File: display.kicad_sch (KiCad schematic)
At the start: 1 part, among them J7 FFC3B11-40-T

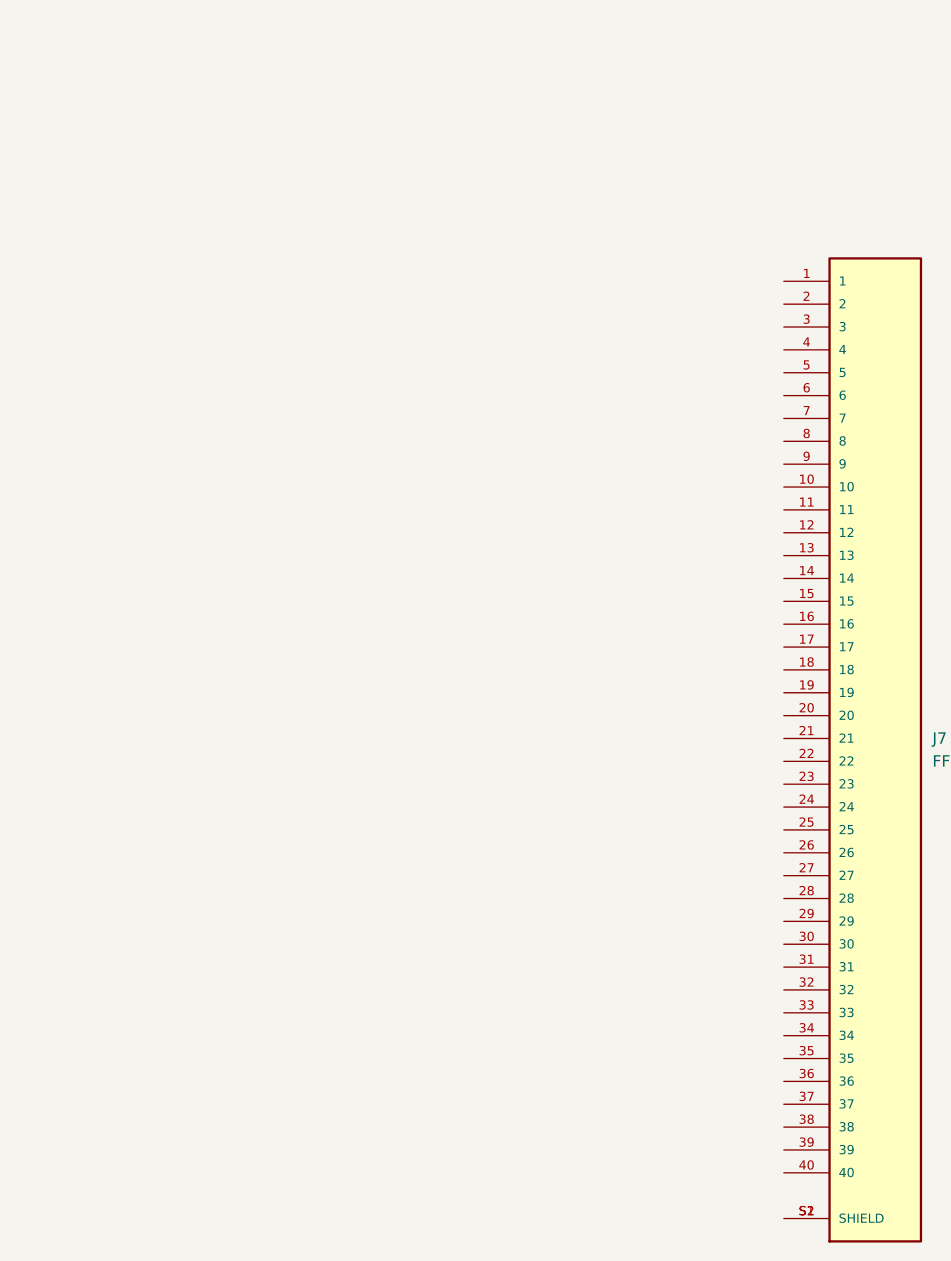
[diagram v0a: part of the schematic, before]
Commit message: Added power supply to LED backlight
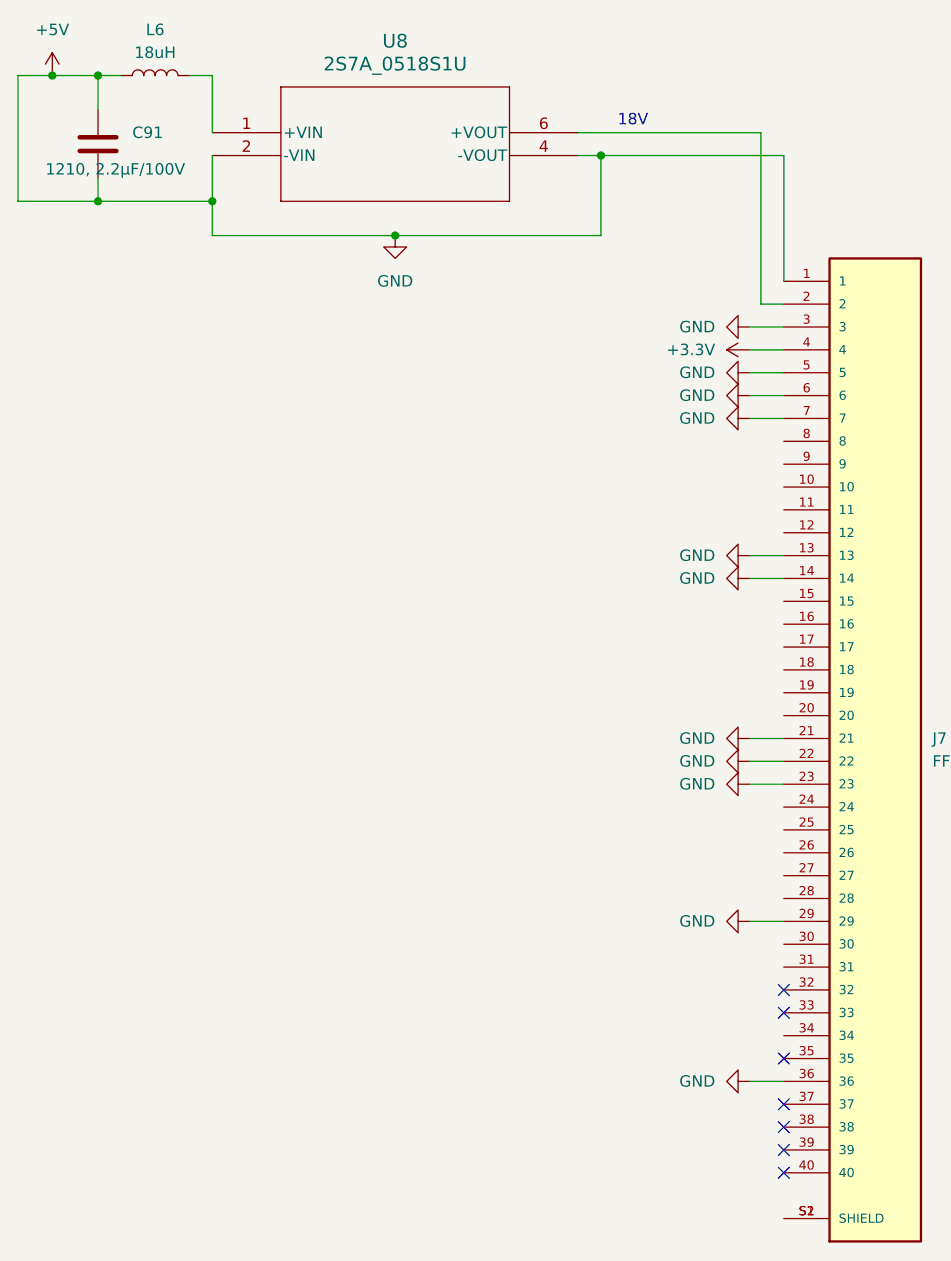
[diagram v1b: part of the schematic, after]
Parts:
- added C91: 1210, 2.2µF/100V, symbol Device:C
- added L6: 18uH, symbol Device:L
- added U8: 2S7A_0518S1U, SIP4_2S7A_GAP, symbol 2S7A_0518S1U:2S7A_0518S1U
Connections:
- net +5V: now reaches J7.1
- net +5V: now also J7.13, J7.14, J7.21, J7.22, J7.23, J7.29, J7.3, J7.36, J7.5, J7.6, J7.7, C91.1, C91.2, L6.1, U8.2 (-VIN), U8.4 (-VOUT)
- net at J7.2: now also U8.6 (+VOUT)
- net +3.3V: now reaches J7.4
- new net: L6.2, U8.1 (+VIN)
- no-connect marks 0 -> 7
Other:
- note added: "18V"

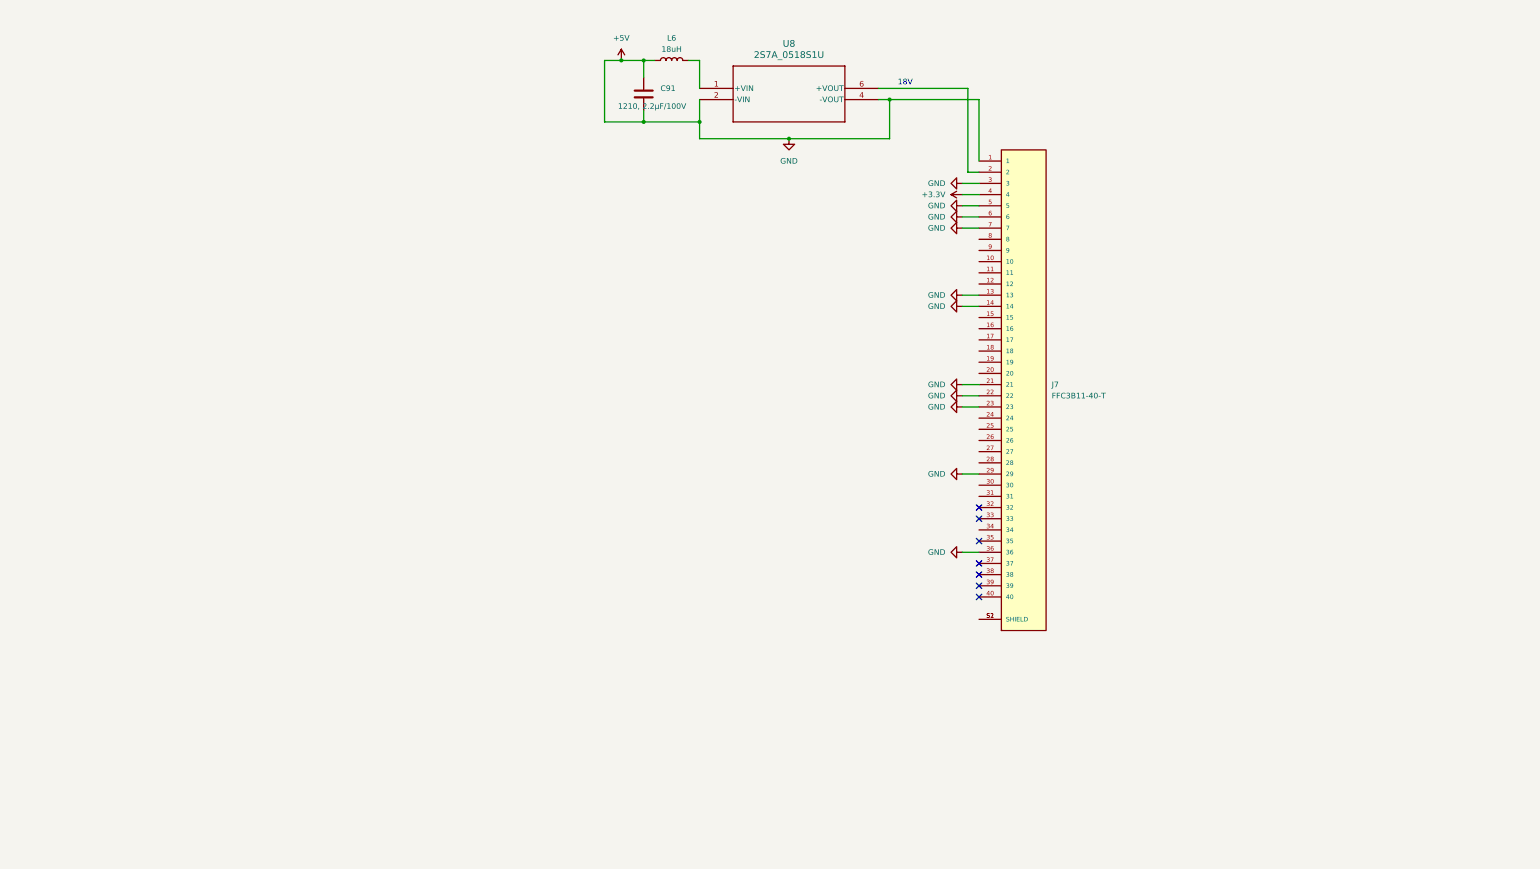
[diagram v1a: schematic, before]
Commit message: Connected controllers and 7-segment display to mcu
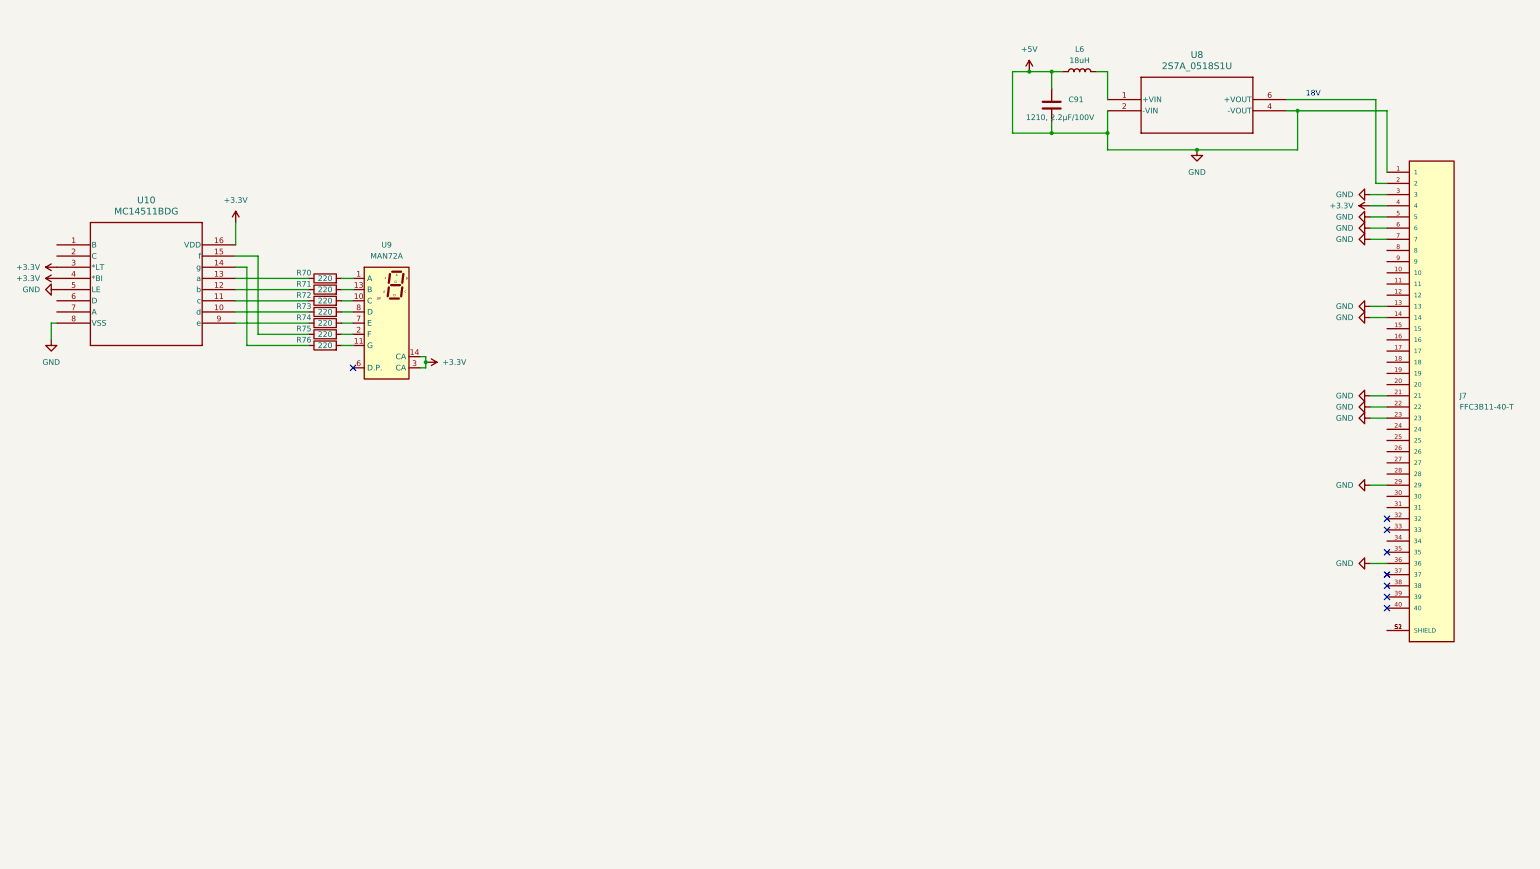
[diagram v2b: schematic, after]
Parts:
- added R70, R71, R72, R73, R74, R75, R76: 220, symbol Device:R
- added U10: MC14511BDG, SOIC-16_ONS, symbol MC14511BDG:MC14511BDG
- added U9: MAN72A, Display_7Segment:MAN72A, symbol Display_Character:MAN72A
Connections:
- net +3.3V: now also U10.16 (VDD), U10.3 (*LT), U10.4 (*BI), U9.14 (CA), U9.3 (CA)
- net +5V: now also U10.5 (LE), U10.8 (VSS)
- new net: R70.2, U9.1 (A)
- new net: R72.2, U9.10 (C)
- new net: R76.2, U9.11 (G)
- new net: R71.2, U9.13 (B)
- new net: R75.2, U9.2 (F)
- new net: R74.2, U9.7 (E)
- new net: R73.2, U9.8 (D)
- new net: R74.1, U10.9 (e)
- new net: R73.1, U10.10 (d)
- new net: R76.1, U10.14 (g)
- new net: R71.1, U10.12 (b)
- new net: R72.1, U10.11 (c)
- new net: R70.1, U10.13 (a)
- new net: R75.1, U10.15 (f)
- no-connect marks 7 -> 8
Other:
- moved on the sheet: C91, J7, L6, U8

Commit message: updated footprints
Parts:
- R70, R71, R72, R73, R74, R75, R76: footprint (none) -> Resistor_SMD:R_0805_2012Metric
- U10: footprint SOIC-16_ONS -> MC14511BDG:SOIC-16_ONS
- U8: footprint SIP4_2S7A_GAP -> 2S7A_0518S1U:SIP4_2S7A_GAP
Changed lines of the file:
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@@
 			)
 		)
-		(property "Footprint" ""
+		(property "Footprint" "Resistor_SMD:R_0805_2012Metric"
 			(at 105.41 117.348 90)
 			(effects
@@
 			)
 		)
-		(property "Footprint" ""
+		(property "Footprint" "Resistor_SMD:R_0805_2012Metric"
 			(at 105.41 114.808 90)
 			(effects
@@
 			)
 		)
-		(property "Footprint" ""
+		(property "Footprint" "Resistor_SMD:R_0805_2012Metric"
 			(at 105.41 122.428 90)
 			(effects
@@
 			)
 		)
-		(property "Footprint" ""
+		(property "Footprint" "Resistor_SMD:R_0805_2012Metric"
 			(at 105.41 109.728 90)
 			(effects
@@
 			)
 		)
-		(property "Footprint" "SOIC-16_ONS"
+		(property "Footprint" "MC14511BDG:SOIC-16_ONS"
 			(at 44.45 97.79 0)
 			(effects
@@
 			)
 		)
-		(property "Footprint" ""
+		(property "Footprint" "Resistor_SMD:R_0805_2012Metric"
 			(at 105.41 107.188 90)
 			(effects
@@
 			)
 		)
-		(property "Footprint" ""
+		(property "Footprint" "Resistor_SMD:R_0805_2012Metric"
 			(at 105.41 119.888 90)
 			(effects
@@
 			)
 		)
-		(property "Footprint" "SIP4_2S7A_GAP"
+		(property "Footprint" "2S7A_0518S1U:SIP4_2S7A_GAP"
 			(at 283.21 64.77 0)
 			(effects
@@
 			)
 		)
-		(property "Footprint" ""
+		(property "Footprint" "Resistor_SMD:R_0805_2012Metric"
 			(at 105.41 112.268 90)
 			(effects

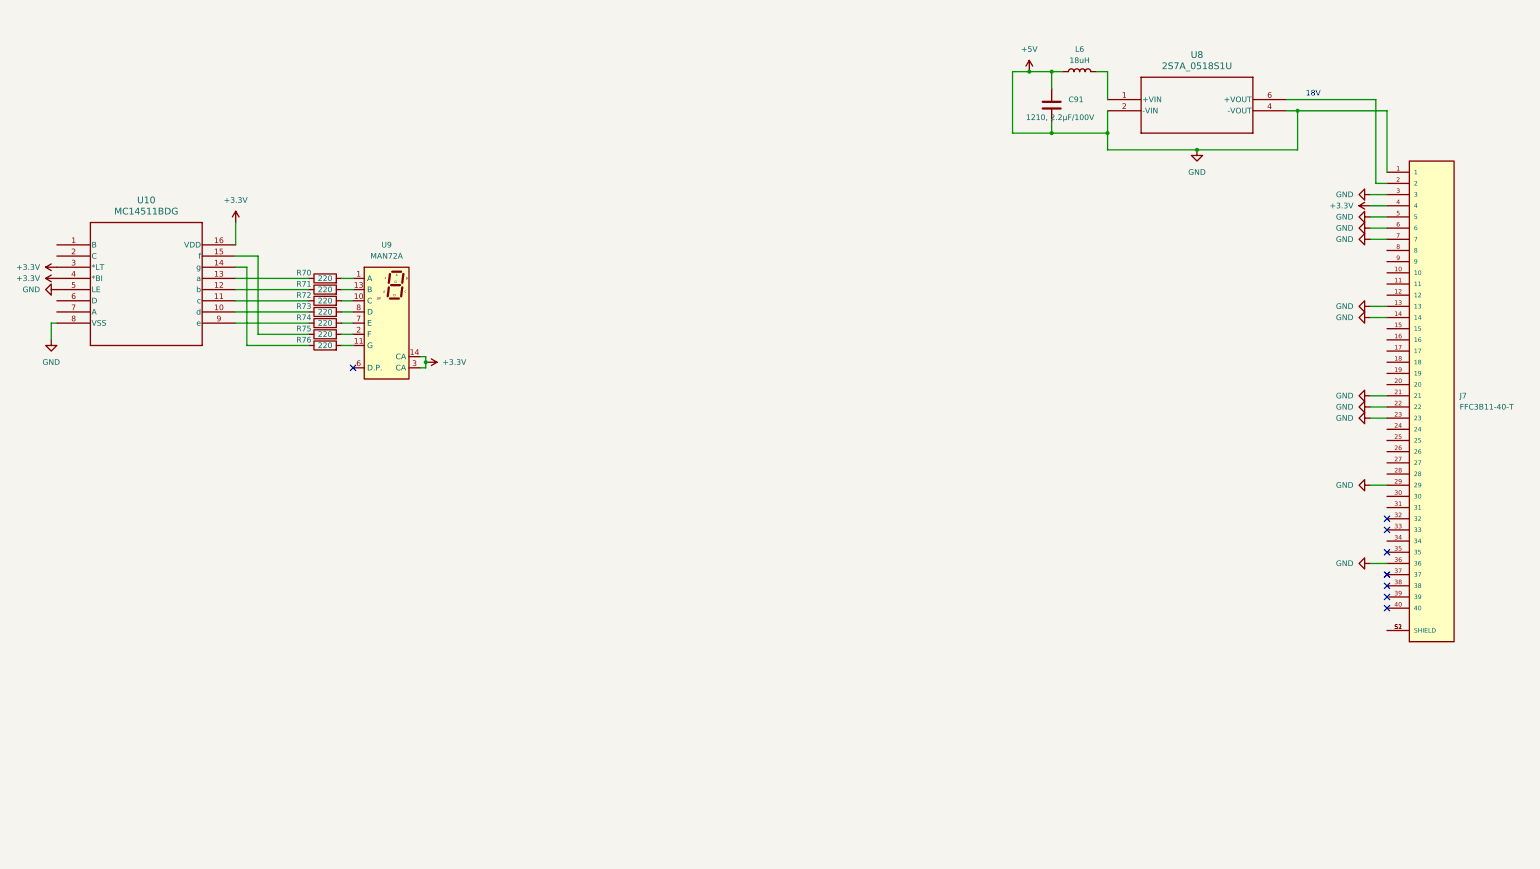
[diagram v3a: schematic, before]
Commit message: Fixed schematic comments
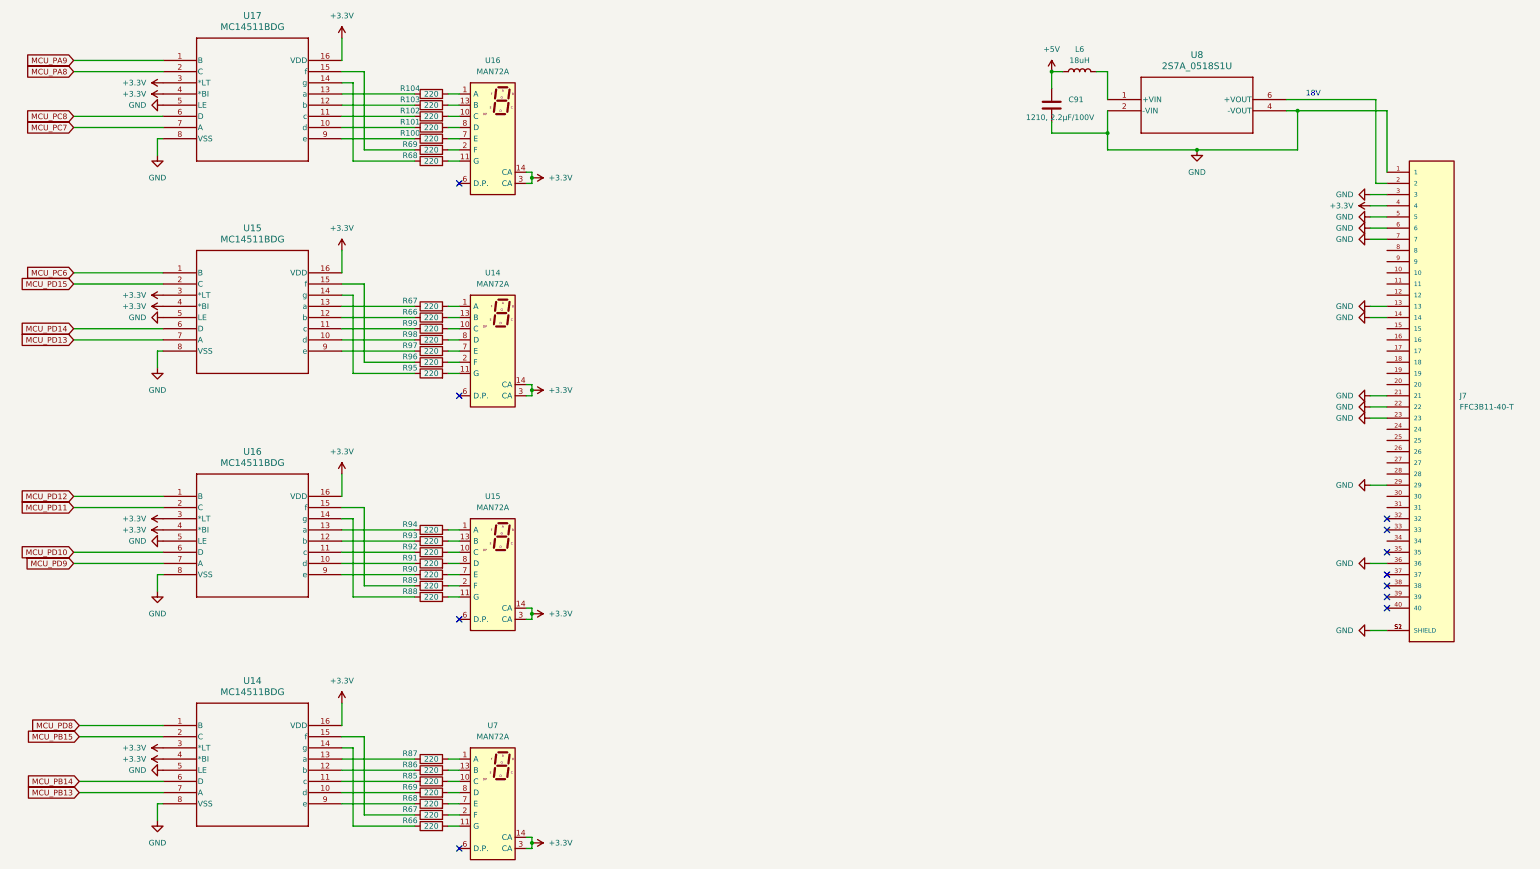
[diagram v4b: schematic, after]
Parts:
- removed R70, R71, R72, R73, R74: 220, Resistor_SMD:R_0805_2012Metric, symbol Device:R
- added R100, R101, R102, R103, R104, R66 (x2), R67 (x2), R68, R69, R85, R86, R87, R88, R89, R90, R91, R92, R93, R94, R95, R96, R97, R98, R99: 220, Resistor_SMD:R_0805_2012Metric, symbol Device:R
- added U14, U15, U7: MAN72A, Display_7Segment:MAN72A, symbol Display_Character:MAN72A
- added U14, U15, U16: MC14511BDG, MC14511BDG:SOIC-16_ONS, symbol MC14511BDG:MC14511BDG
- renumbered R76 to R68, R75 to R69, U9 to U16, U10 to U17
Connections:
- net +3.3V: now also U14.14 (CA), U14.16 (VDD), U14.3 (*LT), U14.3 (CA), U14.4 (*BI), U15.14 (CA), U15.16 (VDD), U15.3 (*LT), U15.3 (CA), U15.4 (*BI), U16.16 (VDD), U16.3 (*LT), U16.4 (*BI), U7.14 (CA), U7.3 (CA)
- net +5V: no longer C91.2, J7.1, J7.13, J7.14, J7.21, J7.22, J7.23, J7.29, J7.3, J7.36, J7.5, J7.6, J7.7, U17.5 (LE), U17.8 (VSS), U8.2 (-VIN), U8.4 (-VOUT)
- net at U16.1 (A): now also R104.2
- net at U16.10 (C): now also R102.2
- net at U16.13 (B): now also R103.2
- net at U16.7 (E): now also R100.2
- net at U16.8 (D): now also R101.2
- net at U17.9 (e): now also R100.1
- net at U17.10 (d): now also R101.1
- net at U17.12 (b): now also R103.1
- net MCU_PA9: now reaches U17.1 (B)
- net at U17.11 (c): now also R102.1
- net at U17.13 (a): now also R104.1
- net MCU_PA8: now reaches U17.2 (C)
- net MCU_PC8: now reaches U17.6 (D)
- net MCU_PC7: now reaches U17.7 (A)
- net GND: now reaches J7.S1 (SHIELD), J7.S2 (SHIELD)
- net GND: now also C91.2, J7.1, J7.13, J7.14, J7.21, J7.22, J7.23, J7.29, J7.3, J7.36, J7.5, J7.6, J7.7, U17.5 (LE), U17.8 (VSS), U8.2 (-VIN), U8.4 (-VOUT), U14.5 (LE), U14.8 (VSS), U15.5 (LE), U15.8 (VSS), U16.5 (LE), U16.8 (VSS)
- new net: R68.1, U14.9 (e)
- new net: R68.2, U7.7 (E)
- new net: R66.1, U14.14 (g)
- new net: R66.2, U7.11 (G)
- new net: R92.1, U16.11 (c)
- new net: R92.2, U15.10 (C)
- new net: R69.1, U14.10 (d)
- new net: R69.2, U7.8 (D)
- new net: R94.1, U16.13 (a)
- new net: R94.2, U15.1 (A)
- new net: R87.1, U14.13 (a)
- new net: R87.2, U7.1 (A)
- new net: R67.2, U14.1 (A)
- new net: R99.2, U14.10 (C)
- new net: R95.2, U14.11 (G)
- new net: R66.2, U14.13 (B)
- new net: R96.2, U14.2 (F)
- new net: R97.2, U14.7 (E)
- new net: R98.2, U14.8 (D)
- new net: R67.1, U15.13 (a)
- new net: R95.1, U15.14 (g)
- new net: R66.1, U15.12 (b)
- new net: R67.1, U14.15 (f)
- new net: R67.2, U7.2 (F)
- new net: R85.1, U14.11 (c)
- new net: R86.1, U14.12 (b)
- new net: R88.1, U16.14 (g)
- new net: R88.2, U15.11 (G)
- new net: R97.1, U15.9 (e)
- new net: R98.1, U15.10 (d)
- new net: R99.1, U15.11 (c)
- new net: R96.1, U15.15 (f)
- new net: R85.2, U7.10 (C)
- new net: R91.1, U16.10 (d)
- new net: R93.1, U16.12 (b)
- new net: R89.1, U16.15 (f)
- new net: R90.1, U16.9 (e)
- new net: R86.2, U7.13 (B)
- new net: R89.2, U15.2 (F)
- new net: R93.2, U15.13 (B)
- new net: R91.2, U15.8 (D)
- new net: R90.2, U15.7 (E)
- new net MCU_PB13: U14.7 (A)
- new net MCU_PB14: U14.6 (D)
- new net MCU_PB15: U14.2 (C)
- new net MCU_PC6: U15.1 (B)
- new net MCU_PD10: U16.6 (D)
- new net MCU_PD11: U16.2 (C)
- new net MCU_PD12: U16.1 (B)
- new net MCU_PD13: U15.7 (A)
- new net MCU_PD14: U15.6 (D)
- new net MCU_PD15: U15.2 (C)
- new net MCU_PD8: U14.1 (B)
- new net MCU_PD9: U16.7 (A)
- no-connect marks 8 -> 11
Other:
- moved on the sheet: R68, R69, U16, U17
